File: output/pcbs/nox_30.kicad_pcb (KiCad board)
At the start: 2 copper layers, 120.3 x 88.1 mm, 70 parts

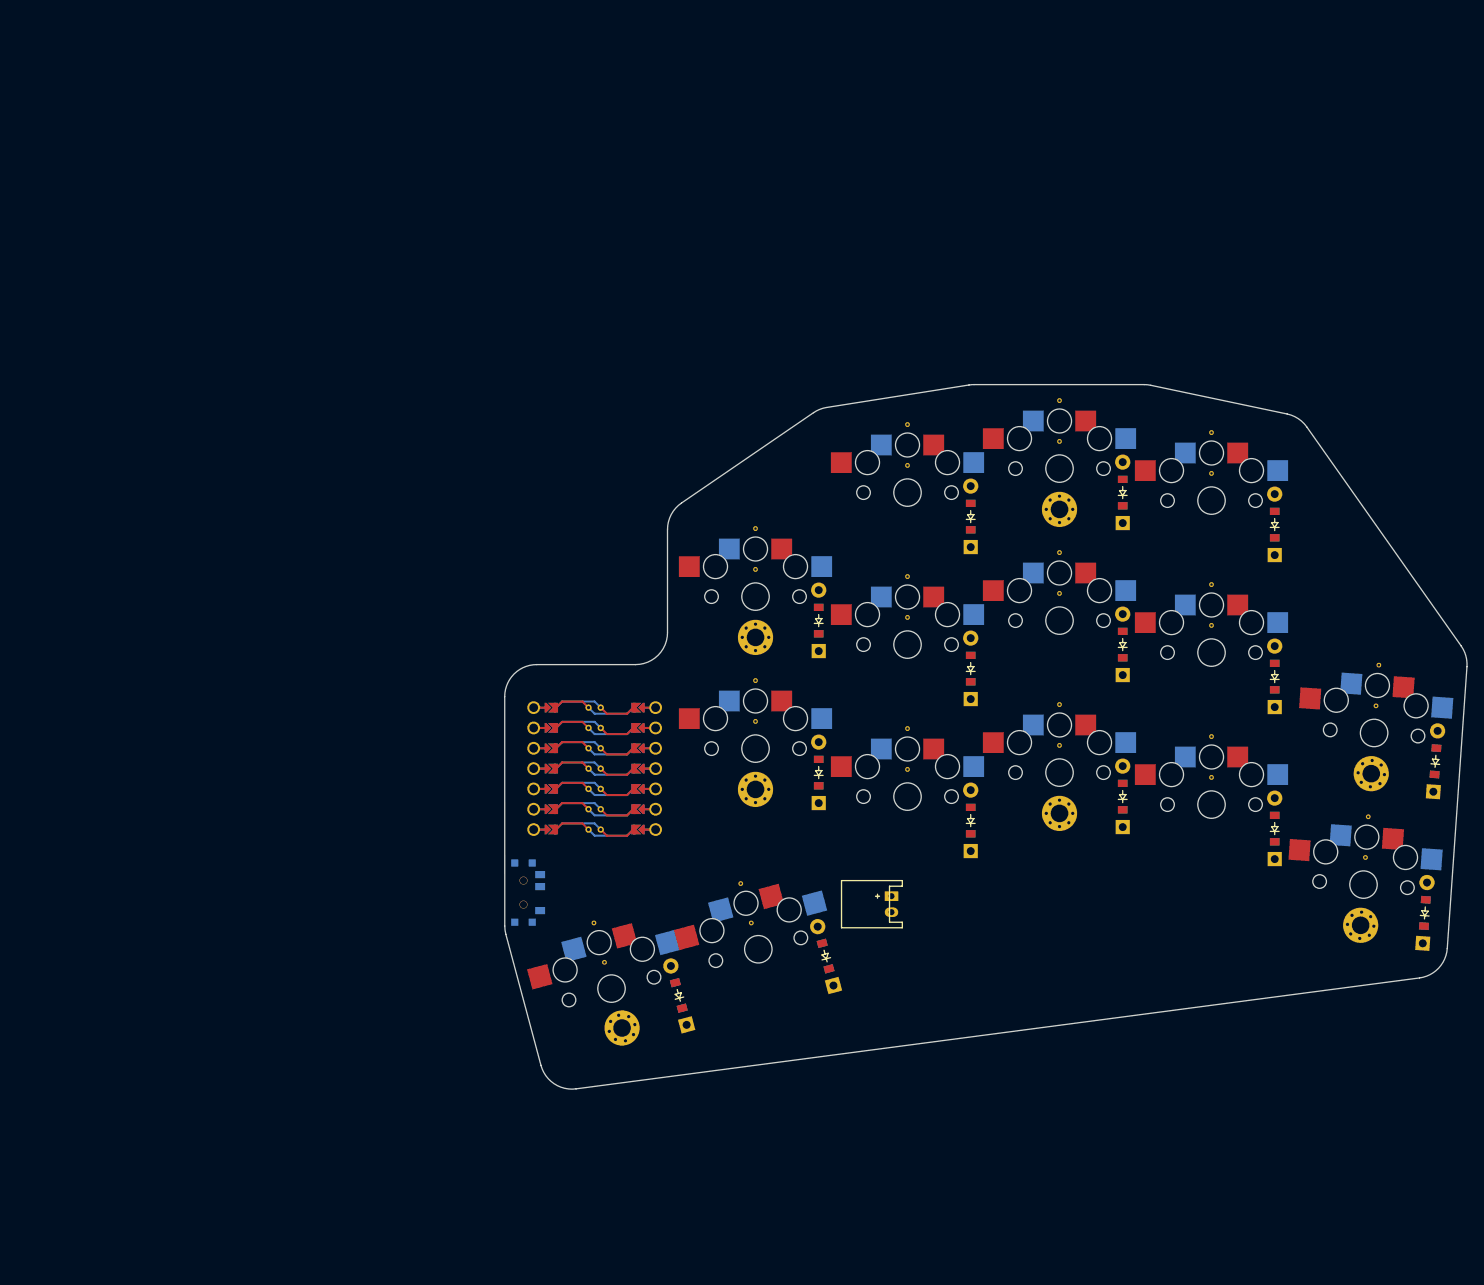
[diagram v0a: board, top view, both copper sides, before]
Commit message: 18 key layout
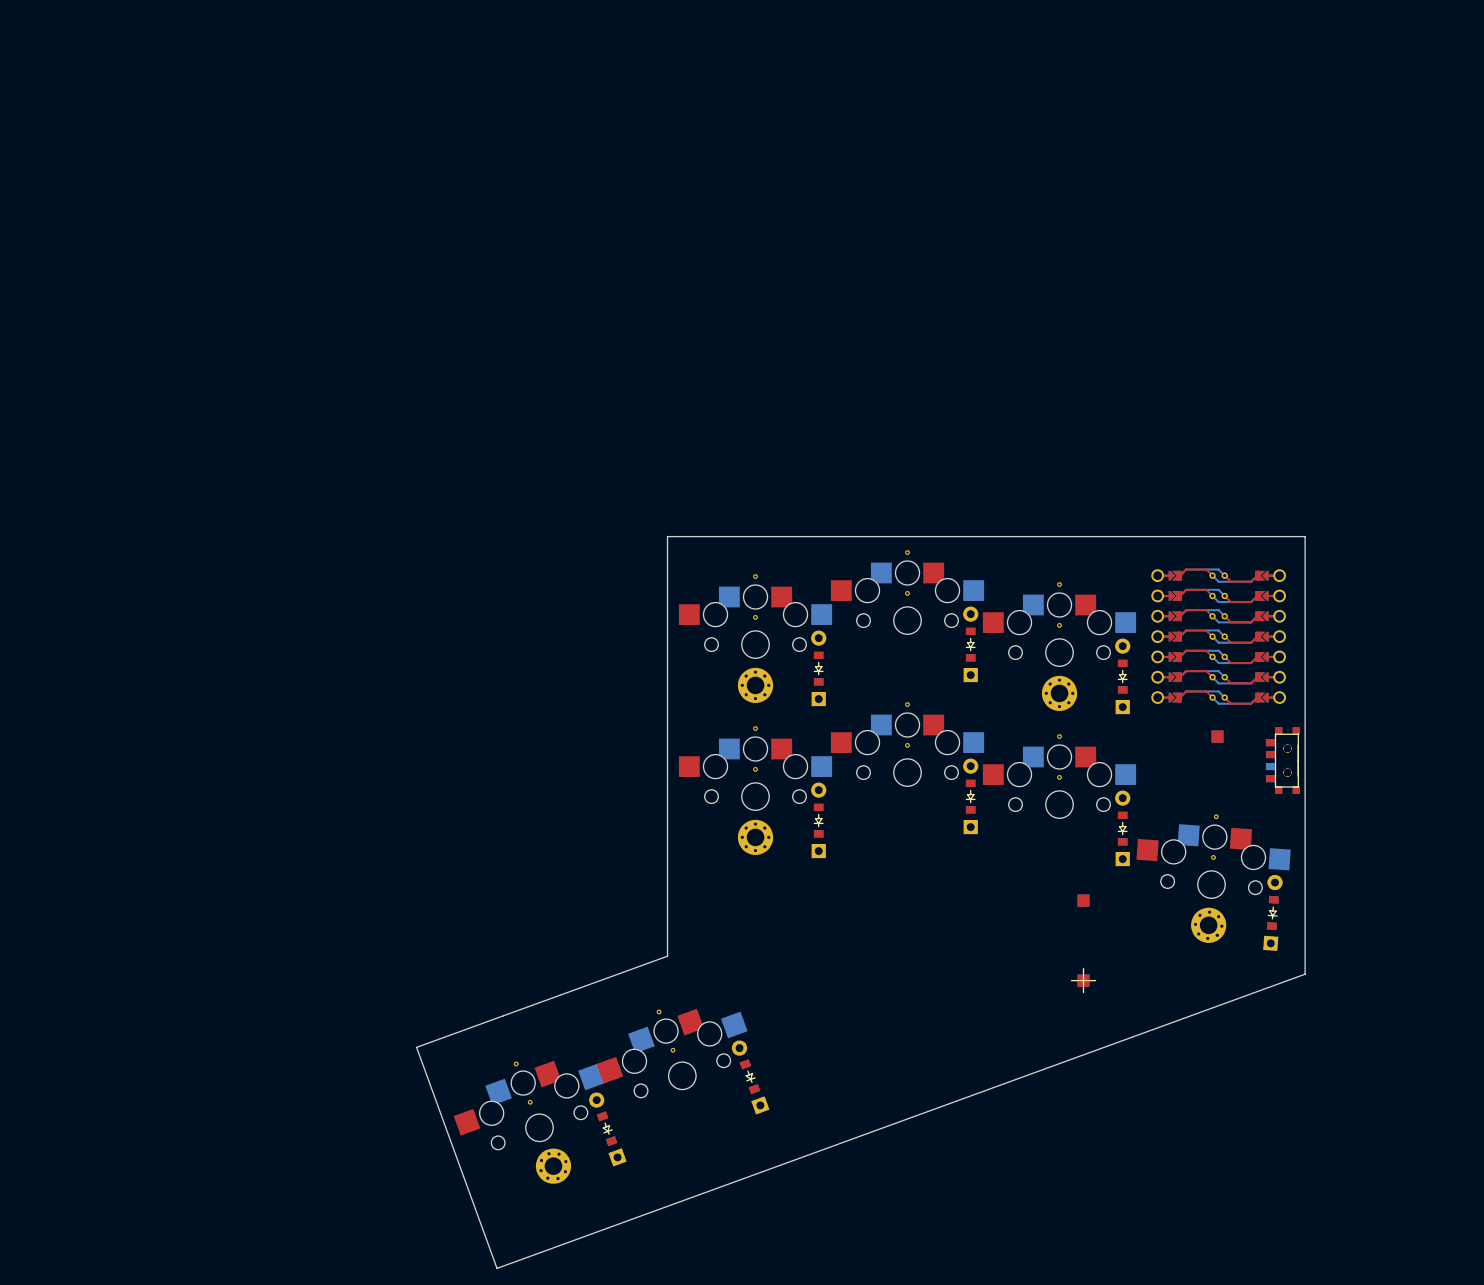
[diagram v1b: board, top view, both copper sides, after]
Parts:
- removed D10, D11, D12, D13, D14, D15: , ComboDiode
- removed JST1: , JST_PH_S2B-PH-K_02x2.00mm_Angled
- removed the REF** at (50.0, 56.5)
- removed the REF** at (107.0, 44.5)
- removed the REF** at (107.0, 25.5)
- removed the REF** at (126.6, 73.5)
- removed the REF** at (127.9, 54.6)
- removed the REF** at (29.8, 86.8)
- removed the REF** at (48.2, 81.9)
- removed the REF** at (50.0, 61.6)
- removed the REF** at (50.0, 42.6)
- removed the REF** at (69.0, 67.6)
- removed the REF** at (69.0, 48.6)
- removed the REF** at (50.0, 37.5)
- removed the REF** at (69.0, 29.6)
- removed the REF** at (88.0, 64.6)
- removed the REF** at (88.0, 45.6)
- removed the REF** at (88.0, 26.6)
- removed the REF** at (107.0, 68.6)
- removed the REF** at (107.0, 49.6)
- removed the REF** at (107.0, 30.6)
- removed the REF** at (126.2, 78.6)
- removed the REF** at (127.6, 59.7)
- removed the REF** at (31.1, 91.7)
- removed the REF** at (69.0, 62.5)
- removed the REF** at (49.5, 86.8)
- removed the REF** at (69.0, 43.5)
- removed the REF** at (69.0, 24.5)
- removed the REF** at (88.0, 59.5)
- removed the REF** at (88.0, 40.5)
- removed the REF** at (88.0, 21.5)
- removed the REF** at (107.0, 63.5)
- removed S10, S11, S12, S13, S14, S15: , PG1350
- removed _31, _32, _33, _34, _35, _36, _37: , MountingHole_2.2mm_M2_Pad_Via
- added BATTPAD1: , ComboDiode, F.Cu at (91.0, 89.0)
- added PAD1: , SMDPad, F.Cu at (107.8, 63.5)
- added REF**: VIA-0.6mm, VIA-0.6mm, F.Cu at (50.0, 62.5)
- added REF**: VIA-0.6mm, VIA-0.6mm, F.Cu at (50.0, 67.6)
- added REF**: VIA-0.6mm, VIA-0.6mm, F.Cu at (50.0, 48.6)
- added REF**: VIA-0.6mm, VIA-0.6mm, F.Cu at (69.0, 64.6)
- added REF**: VIA-0.6mm, VIA-0.6mm, F.Cu at (69.0, 45.6)
- added REF**: VIA-0.6mm, VIA-0.6mm, F.Cu at (88.0, 68.6)
- added REF**: VIA-0.6mm, VIA-0.6mm, F.Cu at (88.0, 49.6)
- added REF**: VIA-0.6mm, VIA-0.6mm, F.Cu at (107.2, 78.6)
- added REF**: VIA-0.6mm, VIA-0.6mm, F.Cu at (21.8, 109.2)
- added REF**: VIA-0.6mm, VIA-0.6mm, F.Cu at (39.7, 102.7)
- added REF**: VIA-0.6mm, VIA-0.6mm, F.Cu at (50.0, 43.5)
- added REF**: VIA-0.6mm, VIA-0.6mm, F.Cu at (69.0, 59.5)
- added REF**: VIA-0.6mm, VIA-0.6mm, F.Cu at (69.0, 40.5)
- added REF**: VIA-0.6mm, VIA-0.6mm, F.Cu at (88.0, 63.5)
- added REF**: VIA-0.6mm, VIA-0.6mm, F.Cu at (88.0, 44.5)
- added REF**: VIA-0.6mm, VIA-0.6mm, F.Cu at (107.6, 73.5)
- added REF**: VIA-0.6mm, VIA-0.6mm, F.Cu at (20.1, 104.4)
- added REF**: VIA-0.6mm, VIA-0.6mm, F.Cu at (37.9, 97.9)
- added T2: , E73:SPDT_C128955, F.Cu at (116.5, 66.5)
- added _19: , MountingHole_2.2mm_M2_Pad_Via, F.Cu at (50.0, 57.1)
- added _20: , MountingHole_2.2mm_M2_Pad_Via, F.Cu at (50.0, 76.1)
- added _21: , MountingHole_2.2mm_M2_Pad_Via, F.Cu at (88.0, 58.1)
- added _22: , MountingHole_2.2mm_M2_Pad_Via, F.Cu at (106.6, 87.1)
- added _23: , MountingHole_2.2mm_M2_Pad_Via, F.Cu at (24.7, 117.2)
- moved S8 105.0 mm to (23.0, 112.4), turned to 20 degrees
- moved D8 102.4 mm to (31.4, 112.5), turned to 110 degrees
- moved T1 96.9 mm to (116.5, 66.5), turned to -90 degrees
- moved xiao-ble1 79.7 mm to (99.0, 61.5)
- moved S9 74.3 mm to (40.9, 105.9), turned to 20 degrees
- moved D9 72.6 mm to (49.3, 106.0), turned to 110 degrees
- moved D5 43.4 mm to (95.9, 75.0)
- moved S5 43.4 mm to (88.0, 72.0)
- moved D7 38.4 mm to (114.7, 85.5), turned to 86 degrees
- moved S7 38.1 mm to (107.0, 82.0), turned to -4 degrees
- moved D6 15.0 mm to (95.9, 56.0)
- moved S6 15.0 mm to (88.0, 53.0)
- moved D1 6.00 mm to (57.9, 74.0)
- moved D2 6.00 mm to (57.9, 55.0)
- moved S1 6.00 mm to (50.0, 71.0)
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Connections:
- D1 pad 1: P8 -> P9
- D1 pad 2: inner_bottom -> index_home
- D2 pad 1: P9 -> P10
- D2 pad 2: inner_home -> index_top
- D3 pad 1: P8 -> P9
- D3 pad 2: index_bottom -> middle_home
- D4 pad 1: P9 -> P10
- D4 pad 2: index_home -> middle_top
- D5 pad 1: P10 -> P9
- D5 pad 2: index_top -> ring_home
- D6 pad 1: P8 -> P10
- D6 pad 2: middle_bottom -> ring_top
- D7 pad 2: middle_home -> pinky_home
- D8 pad 1: P10 -> P8
- D8 pad 2: middle_top -> one_main
- D9 pad 2: ring_bottom -> two_main
- S1 pad 1: inner_bottom -> index_home
- S2 pad 1: inner_home -> index_top
- S3 pad 1: index_bottom -> middle_home
- S4 pad 1: index_home -> middle_top
- S5 pad 1: index_top -> ring_home
- S5 pad 2: P2 -> P3
- S6 pad 1: middle_bottom -> ring_top
- S7 pad 1: middle_home -> pinky_home
- S7 pad 2: P3 -> P4
- S8 pad 1: middle_top -> one_main
- S8 pad 2: P3 -> P1
- S9 pad 1: ring_bottom -> two_main
- S9 pad 2: P4 -> P2
- T1 pad 2: VCC5 -> RAW
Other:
- board size 120.3 x 88.1 mm -> 111.1 x 91.5 mm

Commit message: update case
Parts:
- removed the REF** at (50.0, 62.5)
- removed the REF** at (50.0, 67.6)
- removed the REF** at (50.0, 48.6)
- removed the REF** at (69.0, 64.6)
- removed the REF** at (69.0, 45.6)
- removed the REF** at (88.0, 68.6)
- removed the REF** at (88.0, 49.6)
- removed the REF** at (107.2, 78.6)
- removed the REF** at (21.8, 109.2)
- removed the REF** at (39.7, 102.7)
- removed the REF** at (50.0, 43.5)
- removed the REF** at (69.0, 59.5)
- removed the REF** at (69.0, 40.5)
- removed the REF** at (88.0, 63.5)
- removed the REF** at (88.0, 44.5)
- removed the REF** at (107.6, 73.5)
- removed the REF** at (20.1, 104.4)
- removed the REF** at (37.9, 97.9)
- added REF**: VIA-0.6mm, VIA-0.6mm, F.Cu at (0.00, -2.50)
- added REF**: VIA-0.6mm, VIA-0.6mm, F.Cu at (0.00, 2.60)
- added REF**: VIA-0.6mm, VIA-0.6mm, F.Cu at (0.00, -16.4)
- added REF**: VIA-0.6mm, VIA-0.6mm, F.Cu at (19.0, -0.40)
- added REF**: VIA-0.6mm, VIA-0.6mm, F.Cu at (19.0, -19.4)
- added REF**: VIA-0.6mm, VIA-0.6mm, F.Cu at (38.0, 3.60)
- added REF**: VIA-0.6mm, VIA-0.6mm, F.Cu at (38.0, -15.4)
- added REF**: VIA-0.6mm, VIA-0.6mm, F.Cu at (57.2, 13.6)
- added REF**: VIA-0.6mm, VIA-0.6mm, F.Cu at (-28.2, 44.2)
- added REF**: VIA-0.6mm, VIA-0.6mm, F.Cu at (-10.3, 37.7)
- added REF**: VIA-0.6mm, VIA-0.6mm, F.Cu at (0.00, -21.5)
- added REF**: VIA-0.6mm, VIA-0.6mm, F.Cu at (19.0, -5.50)
- added REF**: VIA-0.6mm, VIA-0.6mm, F.Cu at (19.0, -24.5)
- added REF**: VIA-0.6mm, VIA-0.6mm, F.Cu at (38.0, -1.50)
- added REF**: VIA-0.6mm, VIA-0.6mm, F.Cu at (38.0, -20.5)
- added REF**: VIA-0.6mm, VIA-0.6mm, F.Cu at (57.6, 8.52)
- added REF**: VIA-0.6mm, VIA-0.6mm, F.Cu at (-29.9, 39.4)
- added REF**: VIA-0.6mm, VIA-0.6mm, F.Cu at (-12.1, 32.9)
- moved D9 82.0 mm to (-0.70, 41.0)
- moved D3 82.0 mm to (26.9, 6.00)
- moved D4 82.0 mm to (26.9, -13.0)
- moved D5 82.0 mm to (45.9, 10.0)
- moved D6 82.0 mm to (45.9, -9.00)
- moved D8 82.0 mm to (-18.6, 47.5)
- moved S9 82.0 mm to (-9.15, 40.9)
- moved _22 82.0 mm to (56.6, 22.1)
- moved BATTPAD1 82.0 mm to (41.0, 24.0)
- moved D1 82.0 mm to (7.90, 9.00)
- moved D2 82.0 mm to (7.90, -10.0)
- moved D7 82.0 mm to (64.7, 20.5)
- moved PAD1 82.0 mm to (57.8, -1.50)
- moved S1 82.0 mm to (0.00, 6.00)
- moved S2 82.0 mm to (0.00, -13.0)
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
